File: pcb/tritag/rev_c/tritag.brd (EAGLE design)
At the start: 61 x 34.5 mm, 137 parts, among them J1 TC2030-JLINK-NL, J2 TC2030-JLINK-NL, J3 MICRO_USB_B_HIROSE_ZX62-B-5PA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, J5 BAT_HOLE, J7 CON_MICRO_SDDM3AT-SF-PEJM5, T1 HHM1595A1, U1 NRF52840, U12 SIP32510, U2 MCP73831, U3 FT232RQ, U4 MAX8887EZK33+T, U5 STM32F091CC, U6 SKY13317, U7 LXDC2HN18A, U8 DW1000, U9 LIS2DW12, X1 32MHz, X2 38.4M, X3 16M, X4 32.768kHz

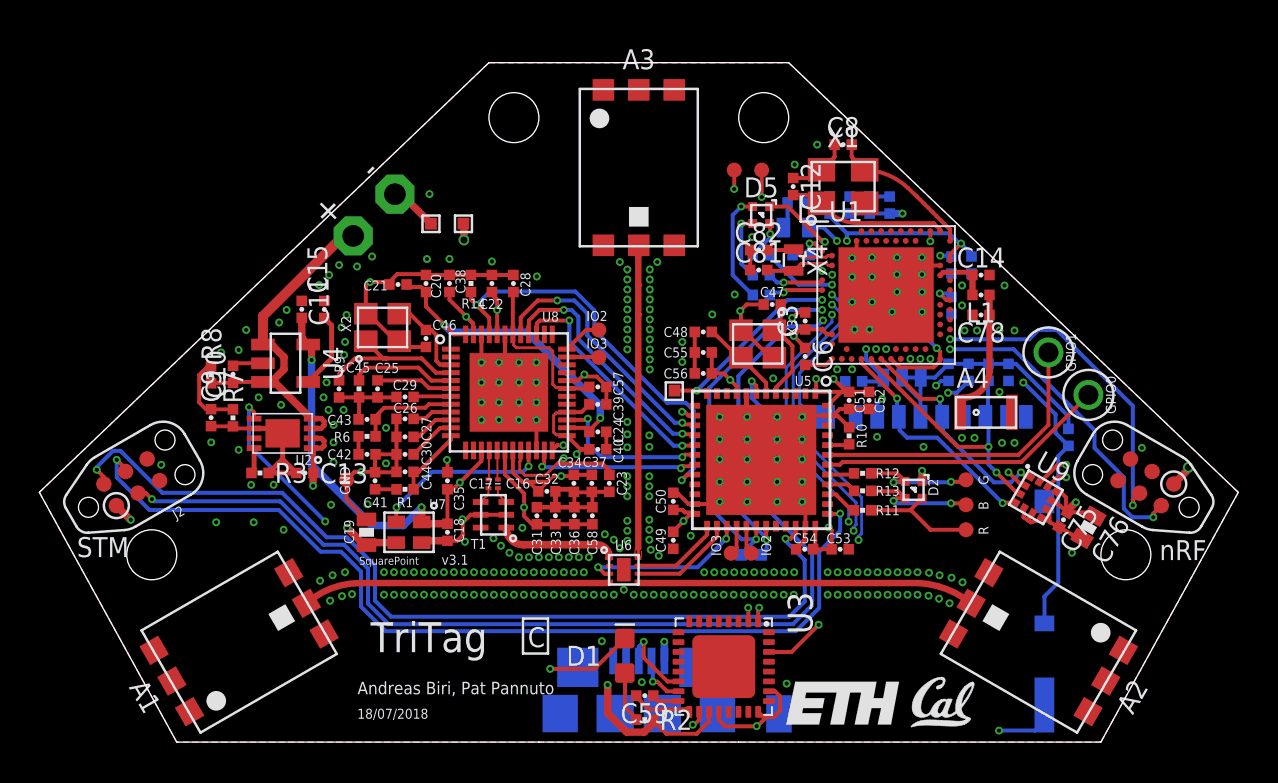
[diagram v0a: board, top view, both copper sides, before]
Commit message: added keepout for BLE antenna; welcome TotTag
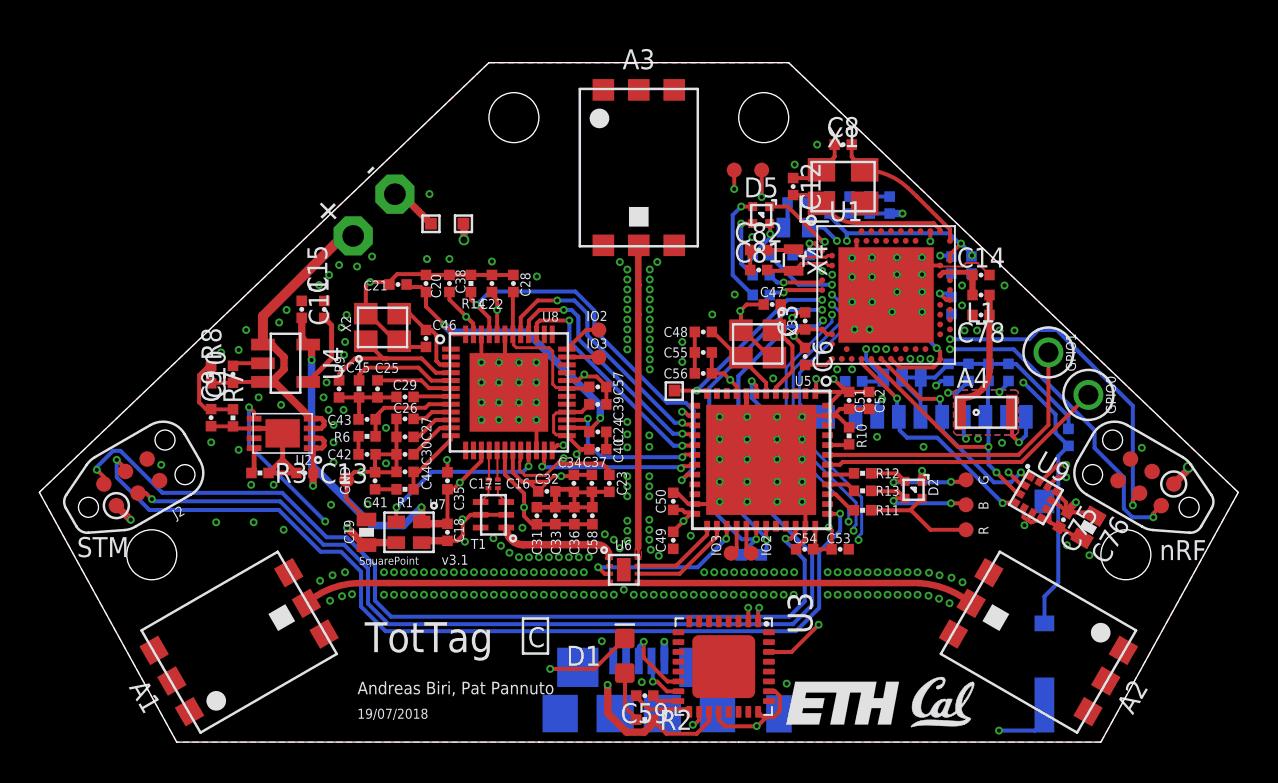
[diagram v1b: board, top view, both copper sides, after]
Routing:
- net GND: track 153.3 -> 161.2 mm, vias 294 -> 297
- added copper zone on layer 1, net N$31
- added copper zone on layer 16, net N$31
- added copper zone on layer 2, net N$31
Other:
- board text added: "19/07/2018"
- board text added: "TotTag"
- board text removed: "18/07/2018"
- board text removed: "TriTag"
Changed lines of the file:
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@@
 <text x="27.66655625" y="6.459396875" size="1.016" layer="21" font="vector" ratio="12" align="top-center">nRF</text>
 <text x="-27.248259375" y="6.611796875" size="1.016" layer="21" font="vector" ratio="12" align="top-center">STM</text>
-<text x="-10.668" y="0.762" size="1.524" layer="21" font="vector" ratio="12" align="bottom-center">TriTag</text>
+<text x="-10.668" y="0.762" size="1.524" layer="21" font="vector" ratio="12" align="bottom-center">TotTag</text>
 <wire x1="-5.886859375" y1="2.471603125" x2="-4.61685625" y2="2.4716" width="0.127" layer="21"/>
 <wire x1="-4.61685625" y1="2.4716" x2="-4.61685625" y2="0.6936" width="0.127" layer="21"/>
@@
 <circle x="13.208" y="28.575" radius="0.127" width="0.1524" layer="51"/>
 <text x="-14.3048" y="-1.0608" size="0.635" layer="21" font="vector" ratio="15" align="center-left">Andreas Biri, Pat Pannuto</text>
-<text x="-14.3144" y="-2.3688" size="0.508" layer="21" font="vector" ratio="12" align="center-left">18/07/2018</text>
+<text x="-14.3144" y="-2.3688" size="0.508" layer="21" font="vector" ratio="12" align="center-left">19/07/2018</text>
 <circle x="14.605" y="27.432" radius="0.127" width="0.1524" layer="51"/>
 <circle x="6.604" y="2.794" radius="0.127" width="0.1524" layer="51"/>
@@
 <via x="16.4338" y="18.3896" extent="1-16" drill="0.2032"/>
 <via x="16.4338" y="19.4056" extent="1-16" drill="0.2032"/>
-<via x="19.1008" y="11.4046" extent="1-16" drill="0.2032"/>
+<via x="19.3294" y="11.43" extent="1-16" drill="0.2032"/>
 <via x="18.4658" y="11.4046" extent="1-16" drill="0.2032"/>
-<via x="17.0688" y="11.6586" extent="1-16" drill="0.2032"/>
-<via x="16.4338" y="11.6586" extent="1-16" drill="0.2032"/>
+<via x="17.2466" y="11.6078" extent="1-16" drill="0.2032"/>
+<via x="16.637" y="11.6078" extent="1-16" drill="0.2032"/>
 <via x="14.478" y="11.2014" extent="1-16" drill="0.2032"/>
-<via x="22.0218" y="5.8166" extent="1-16" drill="0.2032"/>
+<via x="22.9108" y="5.6896" extent="1-16" drill="0.2032"/>
 <via x="25.5778" y="11.1506" extent="1-16" drill="0.2032"/>
 <via x="-24.2824" y="10.287" extent="1-16" drill="0.2032"/>
@@
 <wire x1="18.3134" y1="-3.2258" x2="20.1487125" y2="-3.2258" width="0.2032" layer="16"/>
 <wire x1="20.1487125" y1="-3.2258" x2="20.642465625" y2="-2.732046875" width="0.2032" layer="16"/>
-<wire x1="20.624" y1="-1.923" x2="20.642465625" y2="-2.732046875" width="0" layer="19" extent="16-16"/>
+<via x="16.9418" y="20.9296" extent="1-16" drill="0.2032"/>
+<wire x1="17.22106875" y1="20.55" x2="17.83206875" y2="19.939" width="0.1016" layer="1"/>
+<wire x1="15.3754" y1="20.3706" x2="16.45625625" y2="20.3706" width="0.1016" layer="1"/>
+<wire x1="16.45625625" y1="20.3706" x2="16.63565625" y2="20.55" width="0.1016" layer="1"/>
+<wire x1="16.63565625" y1="20.55" x2="17.22106875" y2="20.55" width="0.1016" layer="1"/>
+<wire x1="15.323" y1="20.423" x2="15.3754" y2="20.3706" width="0.1016" layer="1"/>
+<via x="19.6088" y="7.2136" extent="1-16" drill="0.2032"/>
+<via x="21.7678" y="6.1976" extent="1-16" drill="0.2032"/>
+<wire x1="19.685" y1="11.7856" x2="19.685" y2="12.716" width="0.2032" layer="16"/>
+<wire x1="16.637" y1="11.6078" x2="16.524" y2="11.7208" width="0.2032" layer="16"/>
+<wire x1="16.524" y1="11.7208" x2="16.524" y2="12.727" width="0.2032" layer="16"/>
+<wire x1="18.3388" y1="13.9954" x2="18.796" y2="14.4526" width="0.2032" layer="16"/>
+<wire x1="18.796" y1="14.4526" x2="18.796" y2="14.55293125" width="0.2032" layer="16"/>
+<wire x1="18.978" y1="12.954" x2="18.978" y2="11.7814" width="0.2032" layer="1"/>
+<wire x1="18.978" y1="11.7814" x2="19.3294" y2="11.43" width="0.2032" layer="1"/>
+<wire x1="20.642465625" y1="-2.732046875" x2="20.624" y2="-1.923" width="0" layer="19" extent="16-16"/>
+<wire x1="19.685" y1="12.716" x2="19.674" y2="12.727" width="0.2032" layer="16"/>
+<wire x1="19.3294" y1="11.43" x2="19.685" y2="11.7856" width="0.2032" layer="16"/>
 </signal>
 <signal name="VUSB">
@@
 <wire x1="21.4122" y1="8.2042" x2="21.806534375" y2="7.868046875" width="0.2032" layer="1"/>
 <wire x1="21.806534375" y1="7.868046875" x2="21.717" y2="7.95758125" width="0.2032" layer="1"/>
-<wire x1="21.717" y1="7.95758125" x2="21.717" y2="8.636" width="0.2032" layer="1"/>
-<wire x1="21.717" y1="8.636" x2="21.44248125" y2="8.91051875" width="0.2032" layer="1"/>
-<wire x1="21.44248125" y1="8.91051875" x2="21.21751875" y2="8.91051875" width="0.2032" layer="1"/>
+<wire x1="21.717" y1="7.95758125" x2="21.717" y2="8.382" width="0.2032" layer="1"/>
+<wire x1="21.717" y1="8.382" x2="21.21751875" y2="8.88148125" width="0.2032" layer="1"/>
 <wire x1="9.80308125" y1="6.96091875" x2="9.657790625" y2="7.106209375" width="0.2032" layer="1"/>
 <wire x1="8.3312" y1="7.430134375" x2="9.333865625" y2="7.430134375" width="0.381" layer="15"/>
@@
 <wire x1="-1.651" y1="14.605" x2="-6.019175" y2="18.973175" width="0.381" layer="15"/>
 <wire x1="-6.019175" y1="18.973175" x2="-9.93455625" y2="18.973175" width="0.381" layer="15"/>
+<wire x1="21.21751875" y1="8.88148125" x2="21.21751875" y2="8.91051875" width="0.2032" layer="1"/>
 </signal>
 <signal name="N$22">
@@
 </polygon>
 </signal>
+<signal name="N$31">
+<polygon width="0.0254" layer="2" pour="cutout">
+<vertex x="16.002" y="13.97"/>
+<vertex x="16.002" y="11.938"/>
+<vertex x="16.129" y="11.811"/>
+<vertex x="19.177" y="11.811"/>
+<vertex x="19.304" y="11.938"/>
+<vertex x="19.304" y="13.97"/>
+<vertex x="19.177" y="14.097"/>
+<vertex x="16.129" y="14.097"/>
+</polygon>
+<polygon width="0.0254" layer="16" pour="cutout">
+<vertex x="16.002" y="13.97"/>
+<vertex x="16.002" y="11.938"/>
+<vertex x="16.129" y="11.811"/>
+<vertex x="19.177" y="11.811"/>
+<vertex x="19.304" y="11.938"/>
+<vertex x="19.304" y="13.97"/>
+<vertex x="19.177" y="14.097"/>
+<vertex x="16.129" y="14.097"/>
+</polygon>
+<polygon width="0.0254" layer="1" pour="cutout">
+<vertex x="16.002" y="13.97"/>
+<vertex x="16.002" y="11.938"/>
+<vertex x="16.129" y="11.811"/>
+<vertex x="19.177" y="11.811"/>
+<vertex x="19.304" y="11.938"/>
+<vertex x="19.304" y="13.97"/>
+<vertex x="19.177" y="14.097"/>
+<vertex x="16.129" y="14.097"/>
+</polygon>
+</signal>

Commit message: board done including silk; ready for review
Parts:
- moved U$4 0.13 mm to (13.7, -3.05)
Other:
- board text added: "+3V3"
- board text added: "GPIO 0"
- board text added: "GPIO 1"
- board text added: "SCL"
- board text added: "SDA"

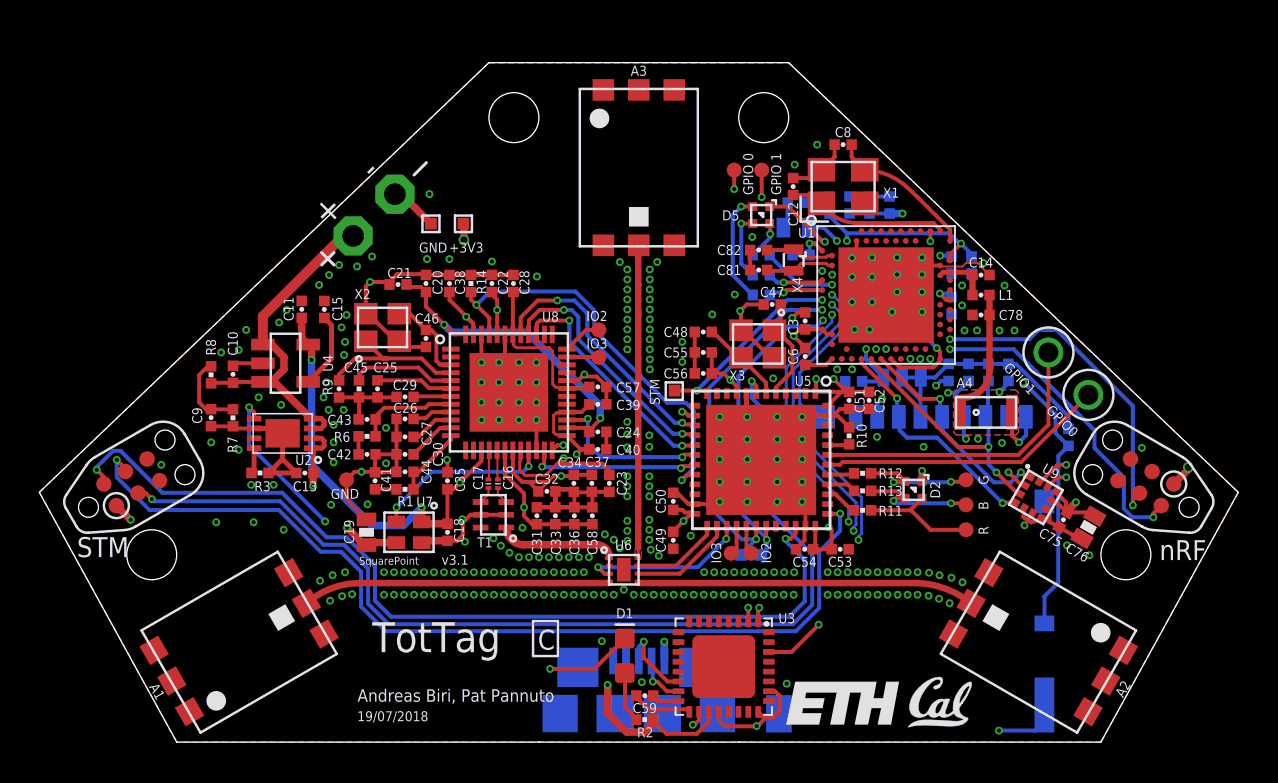
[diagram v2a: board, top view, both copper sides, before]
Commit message: moved BLE antenna and accelerometer and cleaned up nRF connections
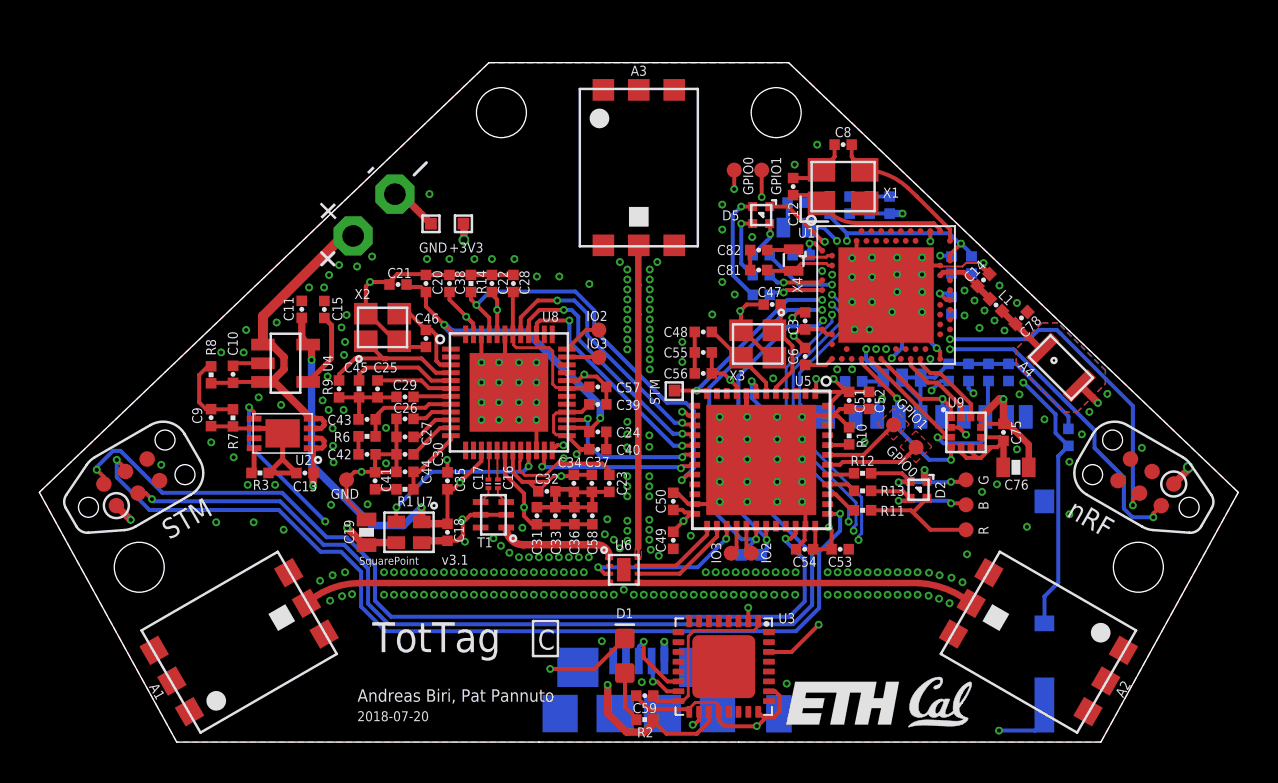
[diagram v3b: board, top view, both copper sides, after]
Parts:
- GPIO0, GPIO1: value TEST_POINT_0.040IN -> TEST-POINT; device headers:TESTPOINT_0.040IN -> headers:PAD.03X.03
- moved GPIO0 9.16 mm to (14.1, 11.2)
- moved GPIO1 8.69 mm to (13.0, 12.3)
- moved C75 5.39 mm to (18.5, 11.9), turned to 270 degrees
- moved U9 4.85 mm to (16.6, 11.9), turned to 0 degrees
- moved C76 4.78 mm to (19.2, 10.2), turned to 180 degrees
- moved A4 4.44 mm to (21.5, 15.2), turned to 315 degrees
- moved C78 2.06 mm to (19.5, 17.8), turned to 45 degrees
- moved L1 0.92 mm to (18.2, 18.4), turned to 135 degrees
- moved C14 0.28 mm to (17.5, 19.7), turned to 45 degrees
- moved D2 0.25 mm to (14.2, 9.02)
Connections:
- net +3V3: no longer U3.1
- net GPIO0: now also GPIO0.P$1; no longer GPIO0.TESTPOINT
- net GPIO1: now also GPIO1.P$1; no longer GPIO1.TESTPOINT
- net N$1: now also U3.1
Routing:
- net GPIO1: track 15.5 -> 3.99 mm
- net GPIO0: track 14.7 -> 4.87 mm
- net NRF_IMU_INT2: track 12.7 -> 4.35 mm, vias 2 -> 0
- net NRF_IMU_INT1: track 12.5 -> 4.34 mm, vias 2 -> 0
- net N$1: track 1.42 -> 9.08 mm
- net NRF_SCK: track 11.4 -> 6.40 mm, vias 2 -> 1
- net N$17: track 6.59 -> 2.86 mm
- net NRF_MOSI: track 14.9 -> 11.3 mm
- net !NRF_CS_IMU: track 12.3 -> 9.23 mm
- net NRF_MISO: track 14.5 -> 12.3 mm, vias 2 -> 1
- net +3V3: track 287.0 -> 285.6 mm
- net !NRF_CS_SD: track 9.16 -> 9.75 mm
- net GND: vias 297 -> 311
- added copper zone on layer 1, net GPIO0
- added copper zone on layer 1, net GPIO1
- added copper zone on layer 15, net N$28
- added copper zone on layer 15, net N$29
- added copper zone on layer 15, net N$30
- added copper zone on layer 15, net N$31
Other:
- board text added: "2018-07-20"
- board text added: "GPIO0"
- board text added: "GPIO1"
- board text removed: "19/07/2018"
- board text removed: "GPIO 0"
- board text removed: "GPIO 1"

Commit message: added clearance for screws, decoupled FT232 to reduce power draw, added power planes
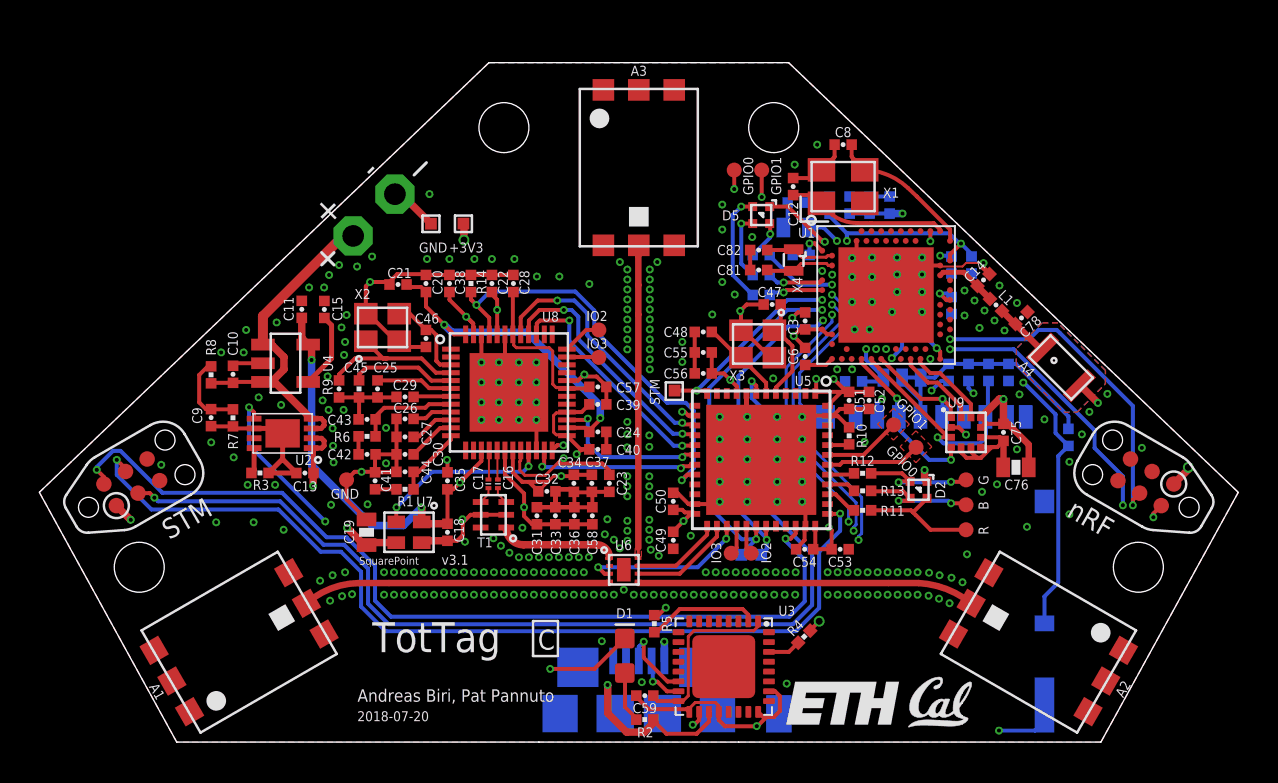
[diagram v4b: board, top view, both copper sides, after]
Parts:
- added R4, R5: 0, passives:0402_RES
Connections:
- new net N$33: R4.1, U3.30
- new net N$34: R5.1, U3.2
- net DBG_RX: now also R4.2; no longer U3.30
- net DBG_TX: now also R5.2; no longer U3.2
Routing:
- net N$34: track 0.00 -> 5.73 mm
- net DBG_TX: track 21.8 -> 26.1 mm
- net DBG_RX: track 23.7 -> 21.2 mm
- net N$33: track 0.00 -> 1.68 mm
- net +3V3: track 285.6 -> 284.6 mm
- net NRF_SWDIO: track 16.1 -> 16.2 mm, vias 2 -> 3
- added copper zone on layer 15, net +1V8
- added copper zone on layer 15, net +3V3
- added copper zone on layer 15, net N$32
- added copper zone on layer 15, net VUSB

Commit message: improved power & ground routing for MCUs, adjusted screw holes and routing around screws, improved distance to RF traces for debugging traces
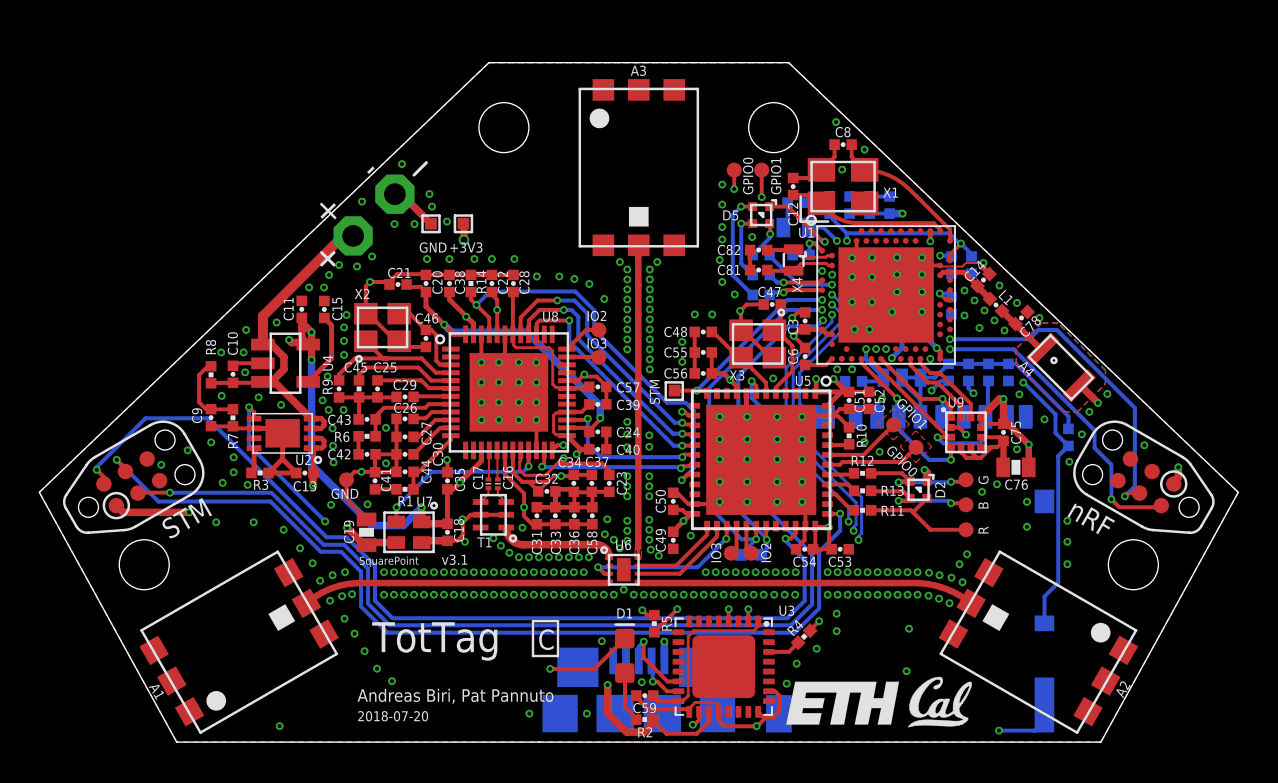
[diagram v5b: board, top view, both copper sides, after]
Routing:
- net +3V3: track 284.6 -> 288.7 mm, vias 23 -> 26
- net DBG_TX: track 26.1 -> 28.1 mm
- net STM_SWDIO: track 46.8 -> 48.2 mm
- net GND: track 161.5 -> 162.1 mm, vias 311 -> 351
- net N$34: track 5.73 -> 6.29 mm, vias 0 -> 2
- net NRF_SWDIO: track 16.2 -> 15.7 mm, vias 3 -> 2
